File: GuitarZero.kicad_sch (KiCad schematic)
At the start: 0 parts

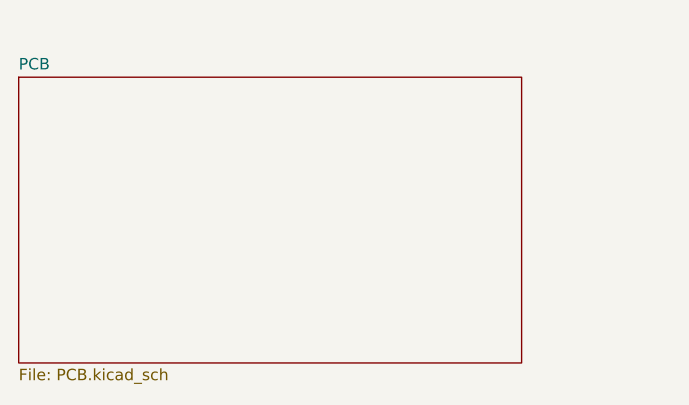
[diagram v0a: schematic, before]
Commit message: Renamed PSU schematic
Was called PCB which was an unhelpful name
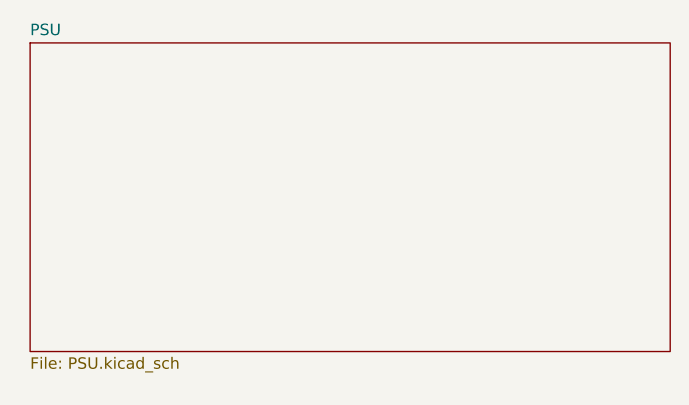
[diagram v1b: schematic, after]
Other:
- removed sheet PCB
- added sheet PSU (PSU.kicad_sch)
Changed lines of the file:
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@@
 (kicad_sch (version 20230121) (generator eeschema)
   (paper "A4")
-  (sheet (at 27.94 29.21) (size 55.88 31.75) (fields_autoplaced)
+  (sheet (at 29.21 25.4) (size 71.12 34.29) (fields_autoplaced)
     (stroke (width 0.1524) (type solid))
     (fill (color 0 0 0 0.0000))
-    (property "Sheetname" "PCB" (at 27.94 28.4984 0)
+    (property "Sheetname" "PSU" (at 29.21 24.6884 0)
       (effects (font (size 1.27 1.27)) (justify left bottom))
     )
-    (property "Sheetfile" "PCB.kicad_sch" (at 27.94 61.5446 0)
+    (property "Sheetfile" "PSU.kicad_sch" (at 29.21 60.2746 0)
       (effects (font (size 1.27 1.27)) (justify left top))
     )

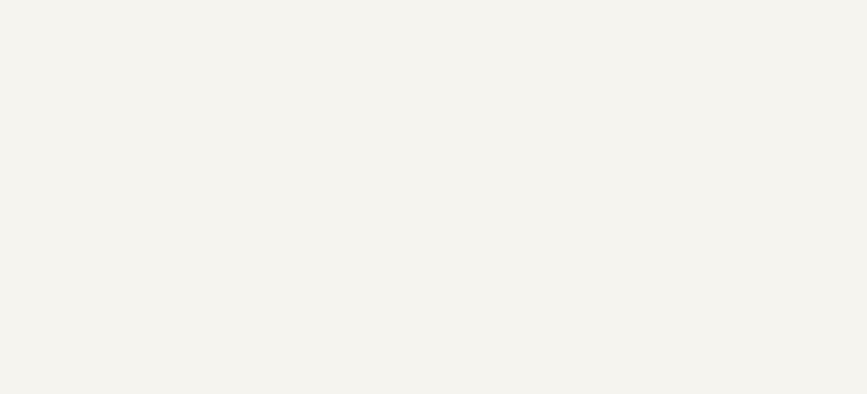
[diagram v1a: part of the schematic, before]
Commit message: Added FPGA schematic with symbol
FPGA symbols seem to big to use currently, so they should be resized.
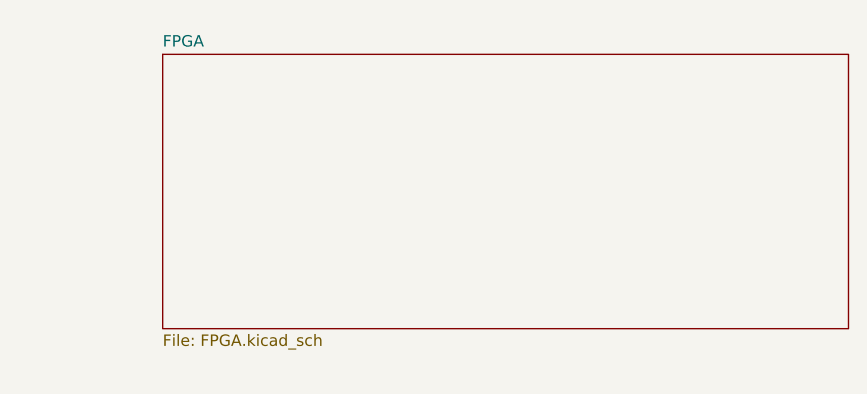
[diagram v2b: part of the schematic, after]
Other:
- added sheet FPGA (FPGA.kicad_sch)
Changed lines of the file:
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@@
+    )
+  )
+  (sheet (at 124.46 26.67) (size 76.2 30.48) (fields_autoplaced)
+    (stroke (width 0.1524) (type solid))
+    (fill (color 0 0 0 0.0000))
+    (property "Sheetname" "FPGA" (at 124.46 25.9584 0)
+      (effects (font (size 1.27 1.27)) (justify left bottom))
+    )
+    (property "Sheetfile" "FPGA.kicad_sch" (at 124.46 57.7346 0)
+      (effects (font (size 1.27 1.27)) (justify left top))
+    )
+    (instances
+      (project "GuitarZero"
+        (path "/fba50eda-8593-4456-af98-ff56fd418a76" (page "3"))
+      )
     )
   )

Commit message: Added MCU schematic
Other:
- added sheet MCU (MCU.kicad_sch)
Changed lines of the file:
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@@
     )
   )
-  (sheet (at 124.46 26.67) (size 76.2 30.48) (fields_autoplaced)
+  (sheet (at 120.65 25.4) (size 76.2 34.29) (fields_autoplaced)
     (stroke (width 0.1524) (type solid))
     (fill (color 0 0 0 0.0000))
-    (property "Sheetname" "FPGA" (at 124.46 25.9584 0)
+    (property "Sheetname" "FPGA" (at 120.65 24.6884 0)
       (effects (font (size 1.27 1.27)) (justify left bottom))
     )
-    (property "Sheetfile" "FPGA.kicad_sch" (at 124.46 57.7346 0)
+    (property "Sheetfile" "FPGA.kicad_sch" (at 120.65 60.2746 0)
       (effects (font (size 1.27 1.27)) (justify left top))
     )
@@
       )
     )
+  )
+  (sheet (at 29.21 71.12) (size 71.12 30.48) (fields_autoplaced)
+    (stroke (width 0.1524) (type solid))
+    (fill (color 0 0 0 0.0000))
+    (property "Sheetname" "MCU" (at 29.21 70.4084 0)
+      (effects (font (size 1.27 1.27)) (justify left bottom))
+    )
+    (property "Sheetfile" "MCU.kicad_sch" (at 29.21 102.1846 0)
+      (effects (font (size 1.27 1.27)) (justify left top))
+    )
+    (instances
+      (project "GuitarZero"
+        (path "/fba50eda-8593-4456-af98-ff56fd418a76" (page "4"))
+      )
+    )

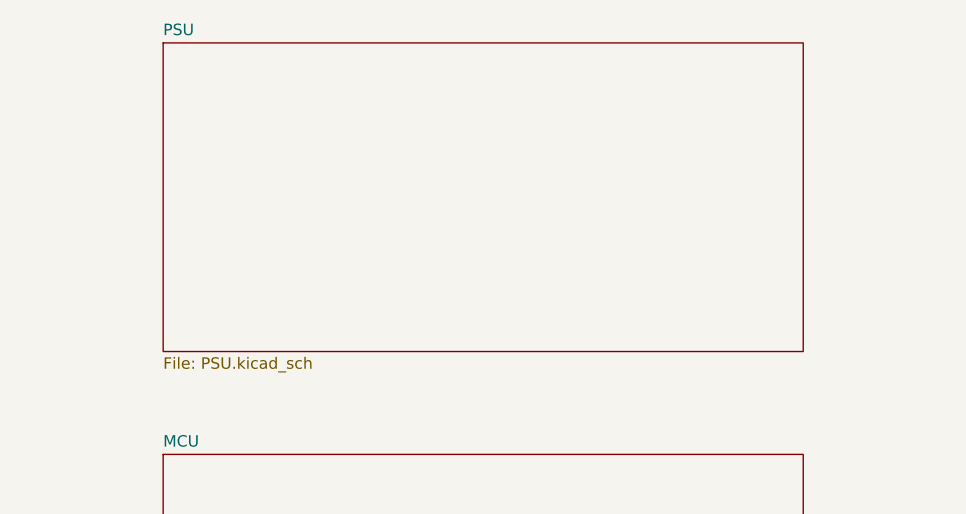
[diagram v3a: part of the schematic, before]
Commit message: Added output pins from PSU schematic
Also renamed FPGA decoupler circuit to not have a typo
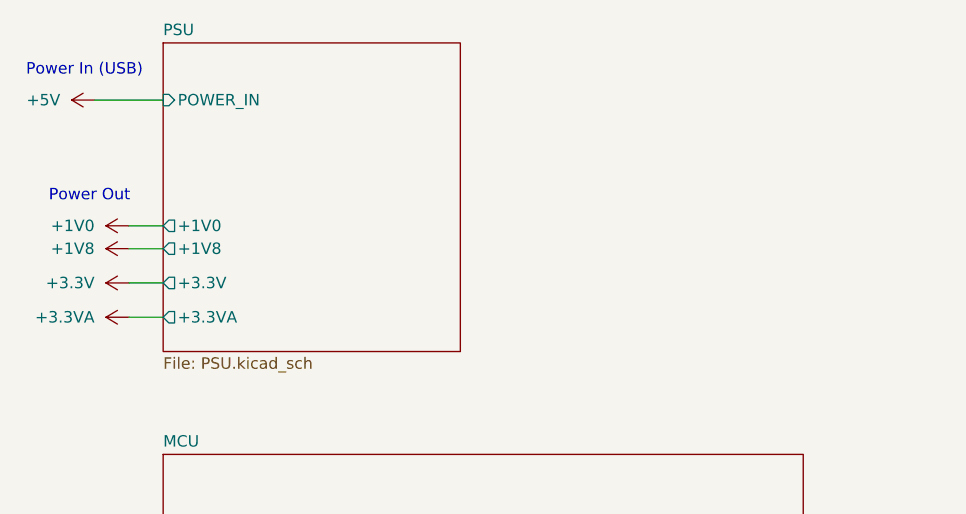
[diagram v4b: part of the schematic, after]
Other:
- sheet PSU ports: added +1V0, +1V8, +3.3V, +3.3VA, POWER_IN; removed none
- note added: "Power In (USB)"
- note added: "Power Out"
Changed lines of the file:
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@@
 (kicad_sch (version 20230121) (generator eeschema)
   (paper "A4")
-  (sheet (at 29.21 25.4) (size 71.12 34.29) (fields_autoplaced)
+  (wire (pts (xy 25.4 55.88) (xy 29.21 55.88))
+    (stroke (width 0) (type default))
+  )
+  (wire (pts (xy 21.59 31.75) (xy 29.21 31.75))
+    (stroke (width 0) (type default))
+  )
+  (wire (pts (xy 25.4 52.07) (xy 29.21 52.07))
+    (stroke (width 0) (type default))
+  )
+  (wire (pts (xy 25.4 48.26) (xy 29.21 48.26))
+    (stroke (width 0) (type default))
+  )
+  (wire (pts (xy 25.4 45.72) (xy 29.21 45.72))
+    (stroke (width 0) (type default))
+  )
+  (text "Power Out" (at 16.51 43.18 0)
+    (effects (font (size 1.27 1.27)) (justify left bottom))
+  )
+  (text "Power In (USB)" (at 13.97 29.21 0)
+    (effects (font (size 1.27 1.27)) (justify left bottom))
+  )
+  (symbol (lib_id "power:+5V") (at 21.59 31.75 90) (unit 1)
+    (in_bom yes) (on_board yes) (dnp no) (fields_autoplaced)
+    (property "Reference" "#PWR015" (at 25.4 31.75 0)
+      (effects (font (size 1.27 1.27)) hide)
+    )
+    (property "Value" "+5V" (at 17.78 31.75 90)
+      (effects (font (size 1.27 1.27)) (justify left))
+    )
+    (property "Footprint" "" (at 21.59 31.75 0)
+      (effects (font (size 1.27 1.27)) hide)
+    )
+    (property "Datasheet" "" (at 21.59 31.75 0)
+      (effects (font (size 1.27 1.27)) hide)
+    )
+    (pin "1")
+    (instances
+      (project "GuitarZero"
+        (path "/fba50eda-8593-4456-af98-ff56fd418a76"
+          (reference "#PWR015") (unit 1)
+        )
+      )
+    )
+  )
+  (symbol (lib_id "power:+1V0") (at 25.4 45.72 90) (unit 1)
+    (in_bom yes) (on_board yes) (dnp no)
+    (property "Reference" "#PWR011" (at 29.21 45.72 0)
+      (effects (font (size 1.27 1.27)) hide)
+    )
+    (property "Value" "+1V0" (at 21.59 45.72 90)
+      (effects (font (size 1.27 1.27)) (justify left))
+    )
+    (property "Footprint" "" (at 25.4 45.72 0)
+      (effects (font (size 1.27 1.27)) hide)
+    )
+    (property "Datasheet" "" (at 25.4 45.72 0)
+      (effects (font (size 1.27 1.27)) hide)
+    )
+    (pin "1")
+    (instances
+      (project "GuitarZero"
+        (path "/fba50eda-8593-4456-af98-ff56fd418a76"
+          (reference "#PWR011") (unit 1)
+        )
+      )
+    )
+  )
+  (symbol (lib_id "power:+3.3VA") (at 25.4 55.88 90) (unit 1)
+    (in_bom yes) (on_board yes) (dnp no)
+    (property "Reference" "#PWR014" (at 29.21 55.88 0)
+      (effects (font (size 1.27 1.27)) hide)
+    )
+    (property "Value" "+3.3VA" (at 21.59 55.88 90)
+      (effects (font (size 1.27 1.27)) (justify left))
+    )
+    (property "Footprint" "" (at 25.4 55.88 0)
+      (effects (font (size 1.27 1.27)) hide)
+    )
+    (property "Datasheet" "" (at 25.4 55.88 0)
+      (effects (font (size 1.27 1.27)) hide)
+    )
+    (pin "1")
+    (instances
+      (project "GuitarZero"
+        (path "/fba50eda-8593-4456-af98-ff56fd418a76"
+          (reference "#PWR014") (unit 1)
+        )
+      )
+    )
+  )
+  (symbol (lib_id "power:+1V8") (at 25.4 48.26 90) (unit 1)
+    (in_bom yes) (on_board yes) (dnp no)
+    (property "Reference" "#PWR012" (at 29.21 48.26 0)
+      (effects (font (size 1.27 1.27)) hide)
+    )
+    (property "Value" "+1V8" (at 21.59 48.26 90)
+      (effects (font (size 1.27 1.27)) (justify left))
+    )
+    (property "Footprint" "" (at 25.4 48.26 0)
+      (effects (font (size 1.27 1.27)) hide)
+    )
+    (property "Datasheet" "" (at 25.4 48.26 0)
+      (effects (font (size 1.27 1.27)) hide)
+    )
+    (pin "1")
+    (instances
+      (project "GuitarZero"
+        (path "/fba50eda-8593-4456-af98-ff56fd418a76"
+          (reference "#PWR012") (unit 1)
+        )
+      )
+    )
+  )
+  (symbol (lib_id "power:+3.3V") (at 25.4 52.07 90) (unit 1)
+    (in_bom yes) (on_board yes) (dnp no)
+    (property "Reference" "#PWR013" (at 29.21 52.07 0)
+      (effects (font (size 1.27 1.27)) hide)
+    )
+    (property "Value" "+3.3V" (at 21.59 52.07 90)
+      (effects (font (size 1.27 1.27)) (justify left))
+    )
+    (property "Footprint" "" (at 25.4 52.07 0)
+      (effects (font (size 1.27 1.27)) hide)
+    )
+    (property "Datasheet" "" (at 25.4 52.07 0)
+      (effects (font (size 1.27 1.27)) hide)
+    )
+    (pin "1")
+    (instances
+      (project "GuitarZero"
+        (path "/fba50eda-8593-4456-af98-ff56fd418a76"
+          (reference "#PWR013") (unit 1)
+        )
+      )
+    )
+  )
+  (sheet (at 29.21 25.4) (size 33.02 34.29) (fields_autoplaced)
     (stroke (width 0.1524) (type solid))
     (fill (color 0 0 0 0.0000))
@@
       (effects (font (size 1.27 1.27)) (justify left top))
     )
+    (pin "POWER_IN" input (at 29.21 31.75 180)
+      (effects (font (size 1.27 1.27)) (justify left))
+    )
+    (pin "+1V8" output (at 29.21 48.26 180)
+      (effects (font (size 1.27 1.27)) (justify left))
+    )
+    (pin "+3.3VA" output (at 29.21 55.88 180)
+      (effects (font (size 1.27 1.27)) (justify left))
+    )
+    (pin "+3.3V" output (at 29.21 52.07 180)
+      (effects (font (size 1.27 1.27)) (justify left))
+    )
+    (pin "+1V0" output (at 29.21 45.72 180)
+      (effects (font (size 1.27 1.27)) (justify left))
+    )
     (instances

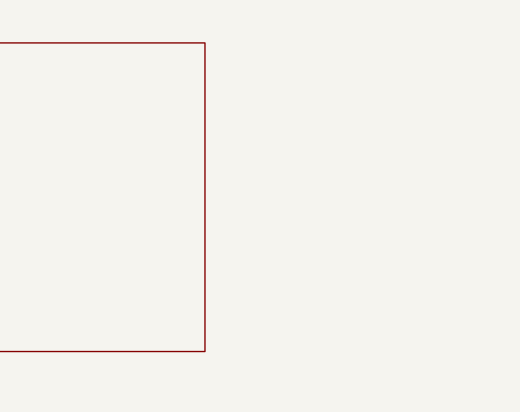
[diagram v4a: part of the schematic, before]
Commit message: Added AudioJack
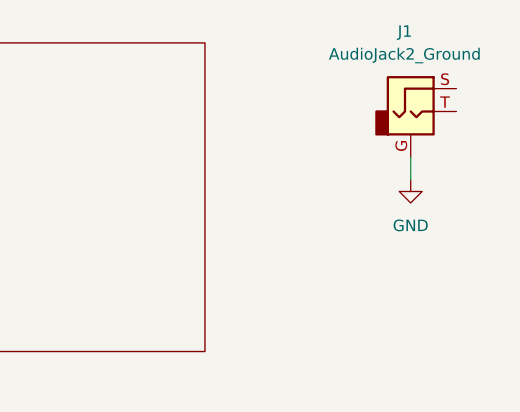
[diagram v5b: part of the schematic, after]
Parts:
- added J1: AudioJack2_Ground, symbol Connector_Audio:AudioJack2_Ground
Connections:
- new net GND: J1.G
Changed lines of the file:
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@@
+    (stroke (width 0) (type default))
+  )
+  (wire (pts (xy 219.71 38.1) (xy 219.71 40.64))
     (stroke (width 0) (type default))
   )
@@
         (path "/fba50eda-8593-4456-af98-ff56fd418a76"
           (reference "#PWR015") (unit 1)
+        )
+      )
+    )
+  )
+  (symbol (lib_id "power:GND") (at 219.71 40.64 0) (unit 1)
+    (in_bom yes) (on_board yes) (dnp no) (fields_autoplaced)
+    (property "Reference" "#PWR033" (at 219.71 46.99 0)
+      (effects (font (size 1.27 1.27)) hide)
+    )
+    (property "Value" "GND" (at 219.71 45.72 0)
+      (effects (font (size 1.27 1.27)))
+    )
+    (property "Footprint" "" (at 219.71 40.64 0)
+      (effects (font (size 1.27 1.27)) hide)
+    )
+    (property "Datasheet" "" (at 219.71 40.64 0)
+      (effects (font (size 1.27 1.27)) hide)
+    )
+    (pin "1")
+    (instances
+      (project "GuitarZero"
+        (path "/fba50eda-8593-4456-af98-ff56fd418a76"
+          (reference "#PWR033") (unit 1)
         )
       )
@@
         )
       )
+    )
+  )
+  (symbol (lib_id "Connector_Audio:AudioJack2_Ground") (at 219.71 33.02 0) (unit 1)
+    (in_bom yes) (on_board yes) (dnp no) (fields_autoplaced)
+    (property "Reference" "J1" (at 219.075 24.13 0)
+      (effects (font (size 1.27 1.27)))
+    )
+    (property "Value" "AudioJack2_Ground" (at 219.075 26.67 0)
+      (effects (font (size 1.27 1.27)))
+    )
+    (property "Footprint" "" (at 219.71 33.02 0)
+      (effects (font (size 1.27 1.27)) hide)
+    )
+    (property "Datasheet" "~" (at 219.71 33.02 0)
+      (effects (font (size 1.27 1.27)) hide)
+    )
+    (pin "G")
+    (pin "S")
+    (pin "T")
+    (instances
+      (project "GuitarZero"
+        (path "/fba50eda-8593-4456-af98-ff56fd418a76"
+          (reference "J1") (unit 1)
+        )
+      )

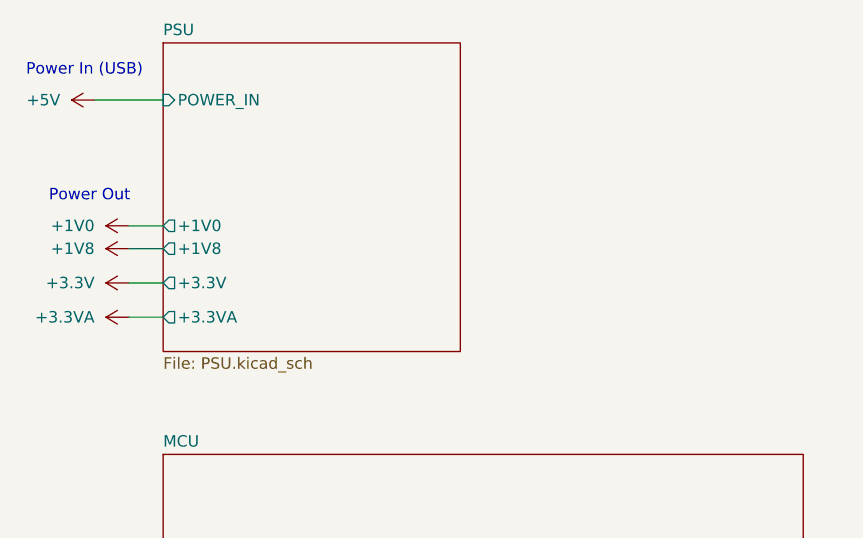
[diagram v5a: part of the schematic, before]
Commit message: Added USB_B_Micro power input
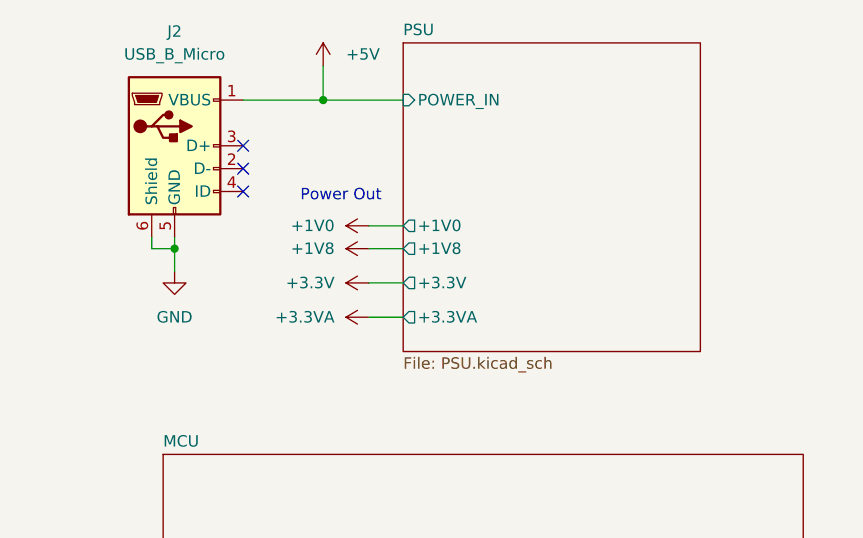
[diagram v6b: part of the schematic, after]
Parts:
- added J2: USB_B_Micro, symbol Connector:USB_B_Micro
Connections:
- net +5V: now also J2.1 (VBUS)
- net GND: now also J2.5 (GND), J2.6 (Shield)
- no-connect marks 0 -> 3
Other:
- note removed: "Power In (USB)"

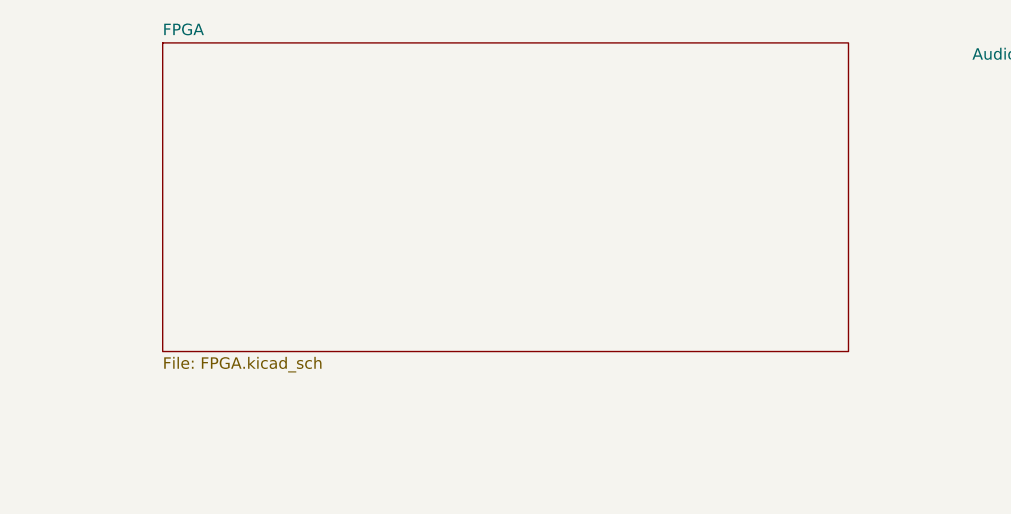
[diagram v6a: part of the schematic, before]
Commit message: Addef outpins for FPGA
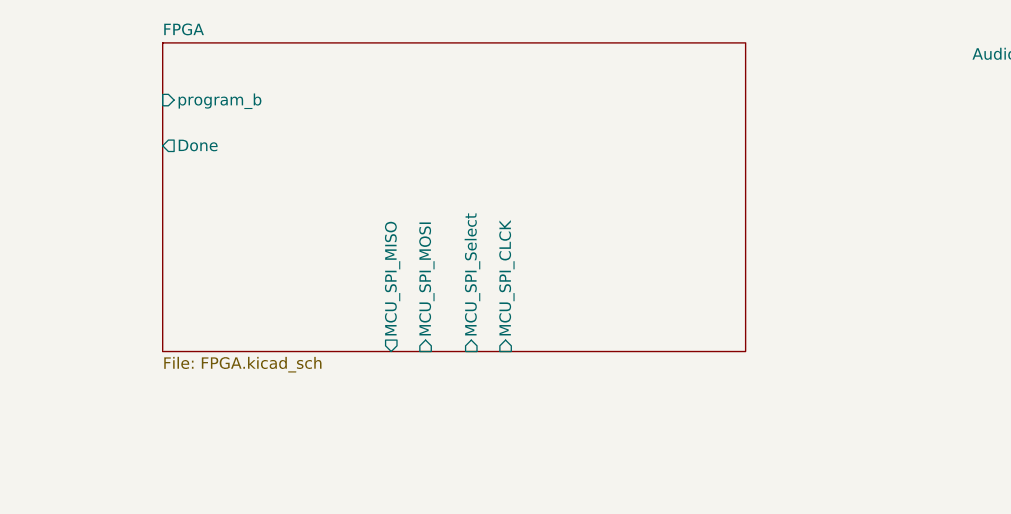
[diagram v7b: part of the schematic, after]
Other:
- sheet FPGA ports: added Done, MCU_SPI_CLCK, MCU_SPI_MISO, MCU_SPI_MOSI, MCU_SPI_Select, program_b; removed none
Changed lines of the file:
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@@
     )
   )
-  (sheet (at 120.65 25.4) (size 76.2 34.29) (fields_autoplaced)
+  (sheet (at 120.65 25.4) (size 64.77 34.29) (fields_autoplaced)
     (stroke (width 0.1524) (type solid))
     (fill (color 0 0 0 0.0000))
@@
       (effects (font (size 1.27 1.27)) (justify left top))
     )
+    (pin "program_b" input (at 120.65 31.75 180)
+      (effects (font (size 1.27 1.27)) (justify left))
+    )
+    (pin "Done" output (at 120.65 36.83 180)
+      (effects (font (size 1.27 1.27)) (justify left))
+    )
+    (pin "MCU_SPI_MISO" output (at 146.05 59.69 270)
+      (effects (font (size 1.27 1.27)) (justify left))
+    )
+    (pin "MCU_SPI_MOSI" input (at 149.86 59.69 270)
+      (effects (font (size 1.27 1.27)) (justify left))
+    )
+    (pin "MCU_SPI_Select" input (at 154.94 59.69 270)
+      (effects (font (size 1.27 1.27)) (justify left))
+    )
+    (pin "MCU_SPI_CLCK" input (at 158.75 59.69 270)
+      (effects (font (size 1.27 1.27)) (justify left))
+    )
     (instances
